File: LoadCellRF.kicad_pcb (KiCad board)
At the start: 2 copper layers, 119 x 58 mm, 7 parts

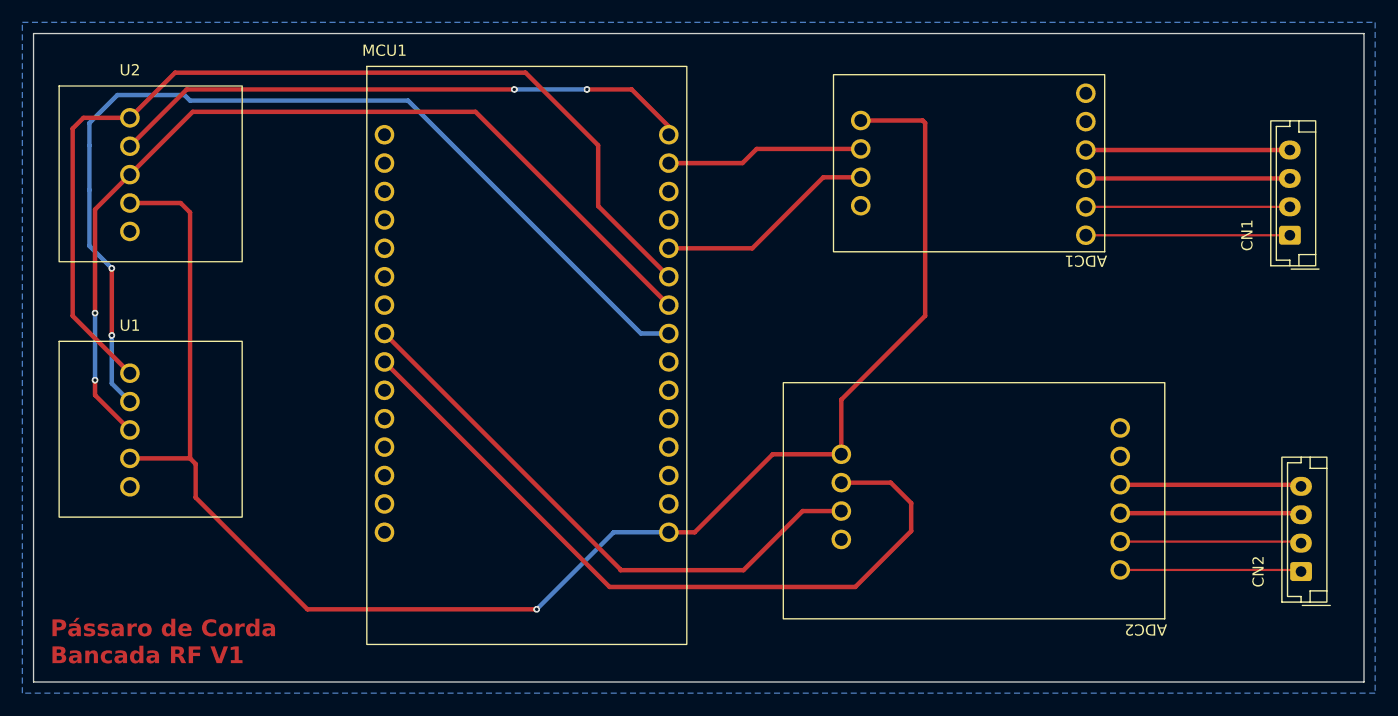
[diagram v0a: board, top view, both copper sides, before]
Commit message: adequate vias for lpkf requirements
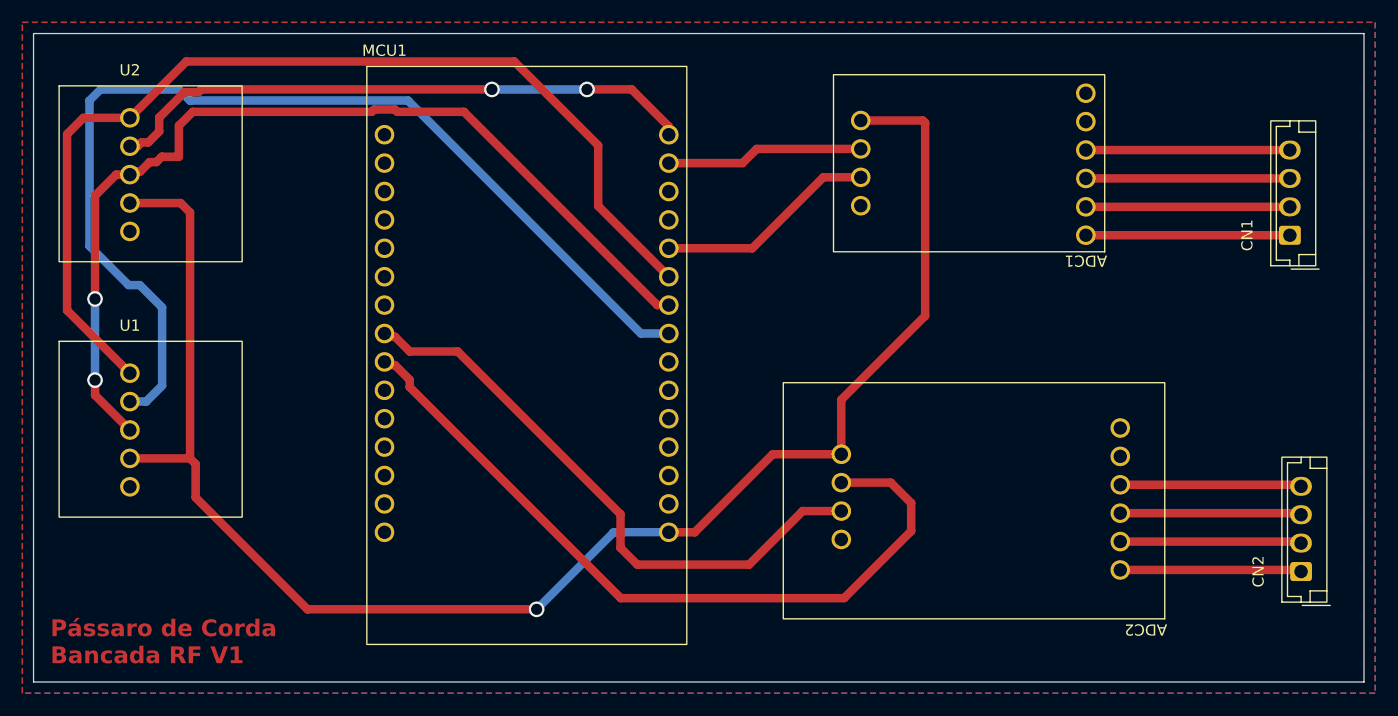
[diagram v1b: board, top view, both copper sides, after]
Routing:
- net /CS1: track 88.1 -> 93.5 mm, vias 2 -> 0
- net /SCK: track 83.1 -> 85.6 mm
- net /DT2: track 51.9 -> 53.2 mm
- net /SO: track 90.1 -> 91.4 mm
- net /SCK2: track 67.0 -> 68.2 mm
- net /CS2: track 52.4 -> 53.1 mm
- added copper zone on F.Cu, net GND

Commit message: change via orientation to cross holes horizontally
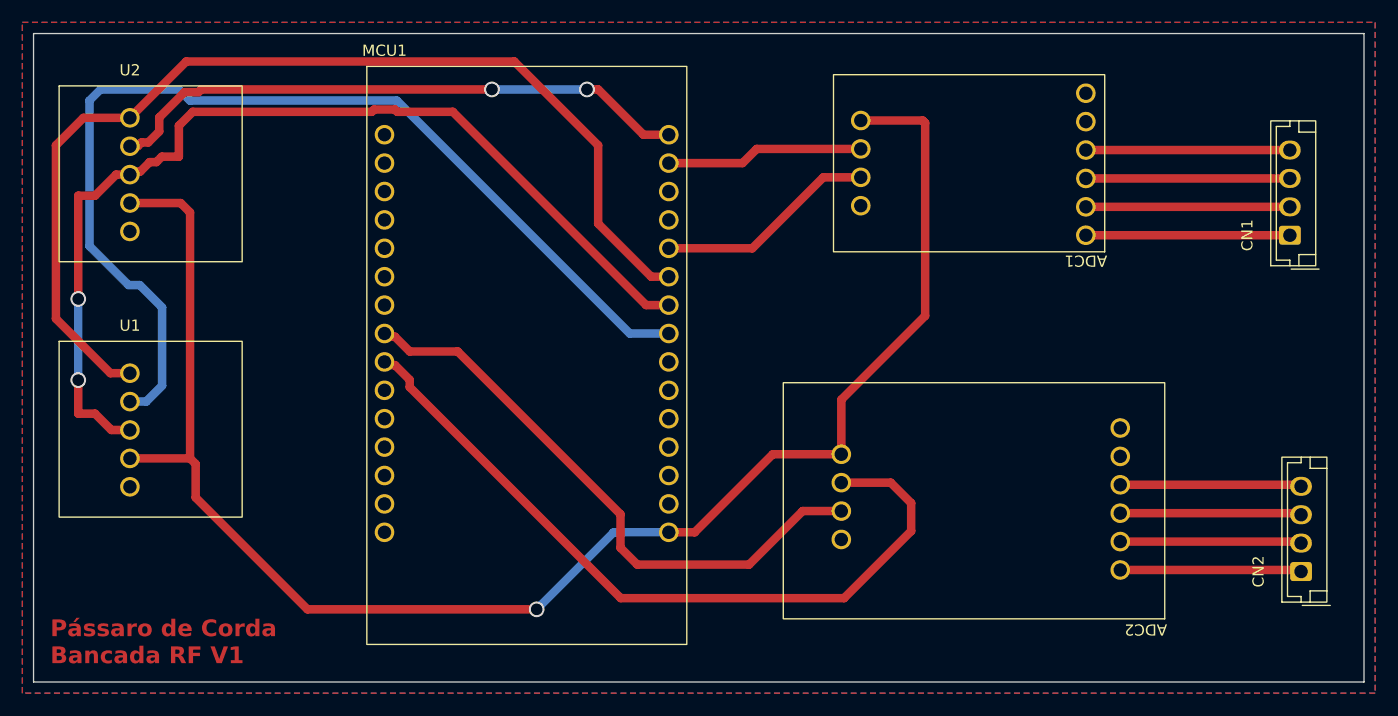
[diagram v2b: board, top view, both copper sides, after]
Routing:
- net /SCK: track 85.6 -> 89.6 mm
- net /SO: track 91.4 -> 94.1 mm
